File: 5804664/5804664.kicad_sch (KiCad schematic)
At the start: 248 parts

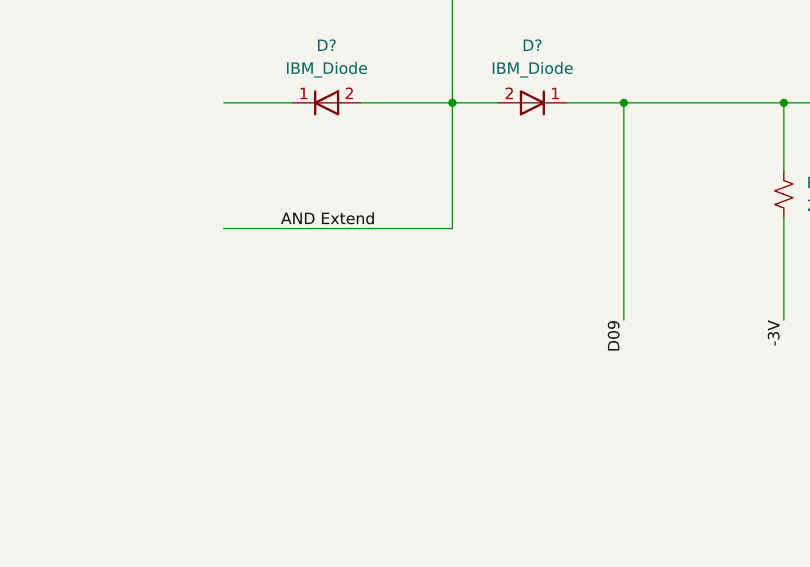
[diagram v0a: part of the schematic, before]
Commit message: Changed input for invert to keep from pulling to 0V
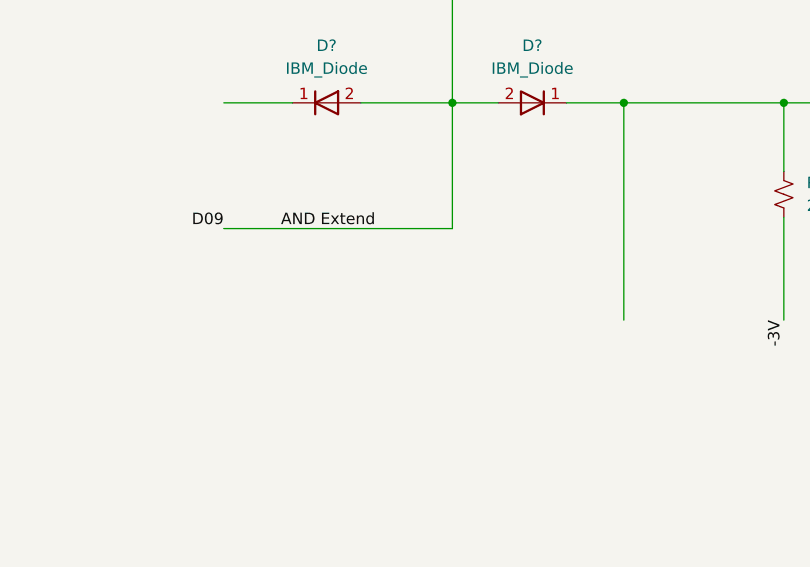
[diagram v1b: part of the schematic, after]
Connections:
- net AND Extend: now also J?.b8 (Pin_b8), R?.2, T?.3 (C)
- net D09: no longer names the net of D?.1 (K), R?.1, T?.1 (B)
- net D09: no longer J?.b8 (Pin_b8), R?.2, T?.3 (C)
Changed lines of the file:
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@@
     (effects (font (size 1.27 1.27)) (justify left bottom))
   )
-  (label "D09" (at 730.25 302.26 270)
+  (label "D09" (at 685.8 292.1 180)
     (effects (font (size 1.27 1.27)) (justify right bottom))
   )
